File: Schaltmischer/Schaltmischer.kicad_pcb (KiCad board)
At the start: 2 copper layers, 13 parts, among them P1 Power, P2 IN, P3 Takt, P4 OUT, T1 Übertrager, T2 Übertrager, U1 FST3125

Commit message: Schaltplan Rev D, Layout Rev A
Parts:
- C1: footprint Capacitors_THT:C_Radial_D6.3_L11.2_P2.5 -> Discret:C1V7H_2
- C2, C3, C4, R1, R2: moved to B.Cu
- moved P1 30.6 mm to (116.8, 96.5)
- moved C4 29.6 mm to (117.4, 92.7)
- moved R1 23.7 mm to (125.1, 94.5), turned to 270 degrees
- moved R2 23.4 mm to (112.4, 94.5), turned to 90 degrees
- moved C3 22.1 mm to (130.8, 88.9)
- moved C1 19.1 mm to (120.7, 90.2), turned to 180 degrees
- moved C2 18.2 mm to (108.0, 88.9), turned to 180 degrees
- moved P3 15.2 mm to (116.8, 73.7)
- moved P4 5.08 mm to (137.2, 81.3)
- moved P2 5.08 mm to (104.1, 81.3)
- moved T1 4.02 mm to (111.8, 82.5), turned to 0 degrees
- moved T2 4.02 mm to (129.5, 82.5), turned to 180 degrees
- moved U1 1.80 mm to (120.7, 82.5)
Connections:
- T1 pad 2: GND -> Net-(C1-Pad1)
- T1 pad 5: Net-(C1-Pad1) -> Net-(T1-Pad5)
- T1 pad 6: Net-(T1-Pad6) -> GND
- T2 pad 1: OUT -> GND
- T2 pad 2: GND -> Net-(C1-Pad1)
- T2 pad 5: Net-(C1-Pad1) -> Net-(T2-Pad5)
- T2 pad 6: Net-(T2-Pad6) -> OUT
- U1 pad 1: SW1 -> SW2
- U1 pad 11: Net-(T2-Pad6) -> Net-(T2-Pad3)
- U1 pad 12: Net-(T1-Pad6) -> Net-(T1-Pad5)
- U1 pad 13: IN1 -> SW1
- U1 pad 2: Net-(T1-Pad3) -> Net-(T1-Pad5)
- U1 pad 3: Net-(T2-Pad3) -> Net-(T2-Pad5)
- U1 pad 4: SW2 -> SW1
- U1 pad 6: Net-(T2-Pad6) -> Net-(T2-Pad5)
- U1 pad 9: Net-(T1-Pad6) -> Net-(T1-Pad3)
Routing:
- net GND: track 0.00 -> 118.9 mm, vias 0 -> 1
- net Net-(C1-Pad1): track 0.00 -> 52.4 mm
- net SW1: track 0.00 -> 20.9 mm, vias 0 -> 1
- net Net-(T1-Pad3): track 0.00 -> 18.5 mm, vias 0 -> 1
- net SW2: track 0.00 -> 17.9 mm, vias 0 -> 2
- net Net-(T1-Pad5): track 0.00 -> 17.7 mm
- net Net-(T2-Pad5): track 0.00 -> 17.1 mm
- net Net-(T2-Pad3): track 0.00 -> 13.5 mm
- net +5V: track 0.00 -> 8.86 mm
- net IN: track 0.00 -> 6.13 mm
- net OUT: track 0.00 -> 6.13 mm
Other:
- net class Default: clearance 0.2 -> 0.2032; trace_width 0.25 -> 0.2032; via_dia 0.6 -> 0.8128; via_drill 0.4 -> 0.4064
- rule trace_clearance: 0.2 -> 0.2032
- rule trace_min: 0.2 -> 0.2032
- rule via_min_drill: 0.3 -> 0.381
- rule via_min_size: 0.4 -> 0.762

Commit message: save before gnd floating
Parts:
- added P5: GND, Mounting_Holes:MountingHole_3.2mm_M3_Pad_Via, F.Cu at (104.6, 74.3)
- added P6: GND, Mounting_Holes:MountingHole_3.2mm_M3_Pad_Via, F.Cu at (136.6, 74.3)
- added P7: GND, Mounting_Holes:MountingHole_3.2mm_M3_Pad_Via, F.Cu at (136.6, 96.3)
- added P8: GND, Mounting_Holes:MountingHole_3.2mm_M3_Pad_Via, F.Cu at (104.6, 96.3)
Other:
- board outline added: 40 x 30 mm

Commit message: save after gnd floating
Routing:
- net GND: track 118.9 -> 2.07 mm
- net +5V: track 8.86 -> 10.6 mm
- added copper zone on B.Cu, net GND
- added copper zone on F.Cu, net GND
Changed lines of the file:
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@@
   (general
     (links 40)
-    (no_connects 4)
-    (area 100.064999 70.204999 141.215001 100.355001)
+    (no_connects 6)
+    (area 100.564999 70.204999 140.715001 100.355001)
     (thickness 1.6)
-    (drawings 15)
-    (tracks 105)
+    (drawings 16)
+    (tracks 84)
     (zones 0)
     (modules 17)
@@
   )
   (setup
-    (last_trace_width 0.2032)
+    (last_trace_width 1.016)
     (user_trace_width 0.254)
     (user_trace_width 0.4064)
@@
     (user_trace_width 1.016)
     (trace_clearance 0.2032)
-    (zone_clearance 0.508)
-    (zone_45_only no)
+    (zone_clearance 0.4)
+    (zone_45_only yes)
     (trace_min 0.2032)
     (segment_width 0.2)
@@
     (pad "" thru_hole circle (at 1.697056 -1.697056) (size 0.6 0.6) (drill 0.5) (layers *.Cu *.Mask))
   )
+  (gr_line (start 116.84 85.09) (end 116.84 86.995) (layer B.Mask) (width 1.016))
   (dimension 7 (width 0.3) (layer Eco1.User)
     (gr_text "7,0 mm" (at 144.99 77.78 90) (layer Eco1.User)
@@
   (gr_line (start 100.64 70.28) (end 140.64 70.28) (layer Edge.Cuts) (width 0.15))
   (gr_line (start 116.84 85.09) (end 115.57 92.71) (layer B.SilkS) (width 1.016))
-  (segment (start 137.16 83.82) (end 134.62 83.82) (width 1.016) (layer B.Cu) (net 1))
-  (segment (start 134.62 83.82) (end 132.08 86.36) (width 1.016) (layer B.Cu) (net 1))
-  (segment (start 132.81 88.9) (end 132.81 87.09) (width 1.016) (layer B.Cu) (net 1))
-  (segment (start 132.81 87.09) (end 132.08 86.36) (width 1.016) (layer B.Cu) (net 1))
-  (segment (start 124.46 87.63) (end 128.905 92.075) (width 0.2032) (layer F.Cu) (net 1))
-  (segment (start 124.46 81.915) (end 124.46 87.63) (width 0.2032) (layer F.Cu) (net 1))
+  (via (at 124.46 81.915) (size 1.2) (drill 0.6) (layers F.Cu B.Cu) (net 1))
   (segment (start 124.46 79.85) (end 124.46 81.915) (width 1.016) (layer B.Cu) (net 1))
-  (via (at 124.46 81.915) (size 1.2) (drill 0.6) (layers F.Cu B.Cu) (net 1))
-  (segment (start 104.14 83.82) (end 106.68 83.82) (width 0.2032) (layer F.Cu) (net 1))
-  (segment (start 106.68 83.82) (end 119.38 96.52) (width 0.2032) (layer F.Cu) (net 1))
-  (segment (start 127.635 71.12) (end 134.62 78.105) (width 0.2032) (layer F.Cu) (net 1))
-  (segment (start 119.38 73.66) (end 121.92 71.12) (width 0.2032) (layer F.Cu) (net 1))
-  (segment (start 121.92 71.12) (end 127.635 71.12) (width 0.2032) (layer F.Cu) (net 1))
-  (segment (start 124.46 96.52) (end 134.62 86.36) (width 0.2032) (layer F.Cu) (net 1))
-  (segment (start 134.62 86.36) (end 137.16 83.82) (width 0.2032) (layer F.Cu) (net 1))
-  (segment (start 134.62 78.105) (end 134.62 86.36) (width 0.2032) (layer F.Cu) (net 1))
-  (segment (start 119.38 96.52) (end 124.46 96.52) (width 0.2032) (layer F.Cu) (net 1))
-  (segment (start 121.92 92.71) (end 121.92 93.98) (width 1.016) (layer B.Cu) (net 1))
-  (segment (start 121.92 93.98) (end 119.38 96.52) (width 1.016) (layer B.Cu) (net 1))
-  (segment (start 119.38 96.52) (end 125.095 96.52) (width 1.016) (layer B.Cu) (net 1))
-  (segment (start 119.38 96.52) (end 119.38 92.71) (width 1.016) (layer B.Cu) (net 1))
-  (segment (start 105.95 88.9) (end 106.68 88.9) (width 1.016) (layer B.Cu) (net 1))
-  (segment (start 106.68 88.9) (end 109.22 86.36) (width 1.016) (layer B.Cu) (net 1))
-  (segment (start 104.14 83.82) (end 106.68 83.82) (width 1.016) (layer B.Cu) (net 1))
-  (segment (start 106.68 83.82) (end 109.22 86.36) (width 1.016) (layer B.Cu) (net 1))
+  (segment (start 119.38 90.17) (end 113.03 90.17) (width 1.016) (layer B.Cu) (net 2))
+  (segment (start 124.46 90.17) (end 119.38 90.17) (width 1.016) (layer B.Cu) (net 2))
   (segment (start 127.54 90.17) (end 125.095 90.17) (width 1.016) (layer B.Cu) (net 2))
   (segment (start 125.095 90.17) (end 124.46 90.17) (width 1.016) (layer B.Cu) (net 2))
@@
   (segment (start 112.395 92.52) (end 112.395 90.17) (width 1.016) (layer B.Cu) (net 2))
   (segment (start 112.395 90.17) (end 111.22 90.17) (width 1.016) (layer B.Cu) (net 2))
-  (segment (start 124.46 90.17) (end 113.03 90.17) (width 1.016) (layer B.Cu) (net 2))
   (segment (start 128.81 88.9) (end 127.54 90.17) (width 1.016) (layer B.Cu) (net 2))
   (segment (start 111.22 90.17) (end 109.95 88.9) (width 1.016) (layer B.Cu) (net 2))
@@
   (segment (start 127 78.74) (end 127 81.28) (width 1.016) (layer B.Cu) (net 2))
   (segment (start 127 81.28) (end 129.54 83.82) (width 1.016) (layer B.Cu) (net 2))
+  (segment (start 116.84 85.25) (end 116.84 86.995) (width 1.016) (layer B.Cu) (net 3))
   (segment (start 112.395 96.52) (end 116.84 96.52) (width 1.016) (layer B.Cu) (net 3))
   (segment (start 116.84 96.52) (end 116.84 94.17) (width 1.016) (layer B.Cu) (net 3))
@@
   (segment (start 129.54 78.74) (end 129.54 77.67934) (width 1.016) (layer B.Cu) (net 11))
   (segment (start 129.54 77.67934) (end 128.69566 76.835) (width 1.016) (layer B.Cu) (net 11))
+  (zone (net 1) (net_name GND) (layer F.Cu) (hatch edge 0.508)
+    (connect_pads yes (clearance 0.4))
+    (min_thickness 1.5)
+    (fill yes (arc_segments 16) (thermal_gap 0.508) (thermal_bridge_width 0.508) (smoothing fillet))
+    (polygon
+      (pts
+        (xy 100.64 70.28) (xy 140.64 70.28) (xy 140.64 100.28) (xy 100.64 100.28)
+      )
+    )
+  )
+  (zone (net 1) (net_name GND) (layer B.Cu) (hatch edge 0.508)
+    (connect_pads yes (clearance 0.4))
+    (min_thickness 1.5)
+    (fill yes (arc_segments 16) (thermal_gap 0.508) (thermal_bridge_width 0.508) (smoothing fillet))
+    (polygon
+      (pts
+        (xy 100.64 70.28) (xy 140.64 70.28) (xy 140.64 100.28) (xy 100.64 100.28)
+      )
+    )
+  )
+  (zone (net 0) (net_name "") (layer B.Cu) (hatch edge 0.508)
+    (connect_pads yes (clearance 0.4))
+    (min_thickness 1.5)
+    (keepout (tracks allowed) (vias allowed) (copperpour not_allowed))
+    (fill yes (arc_segments 16) (thermal_gap 0.508) (thermal_bridge_width 0.508) (smoothing fillet))
+    (polygon
+      (pts
+        (xy 110.49 86.36) (xy 130.81 86.36) (xy 130.81 83.82) (xy 133.35 83.82) (xy 133.35 77.47)
+        (xy 107.95 77.47) (xy 107.95 83.82) (xy 110.49 83.82)
+      )
+    )
+  )
 )

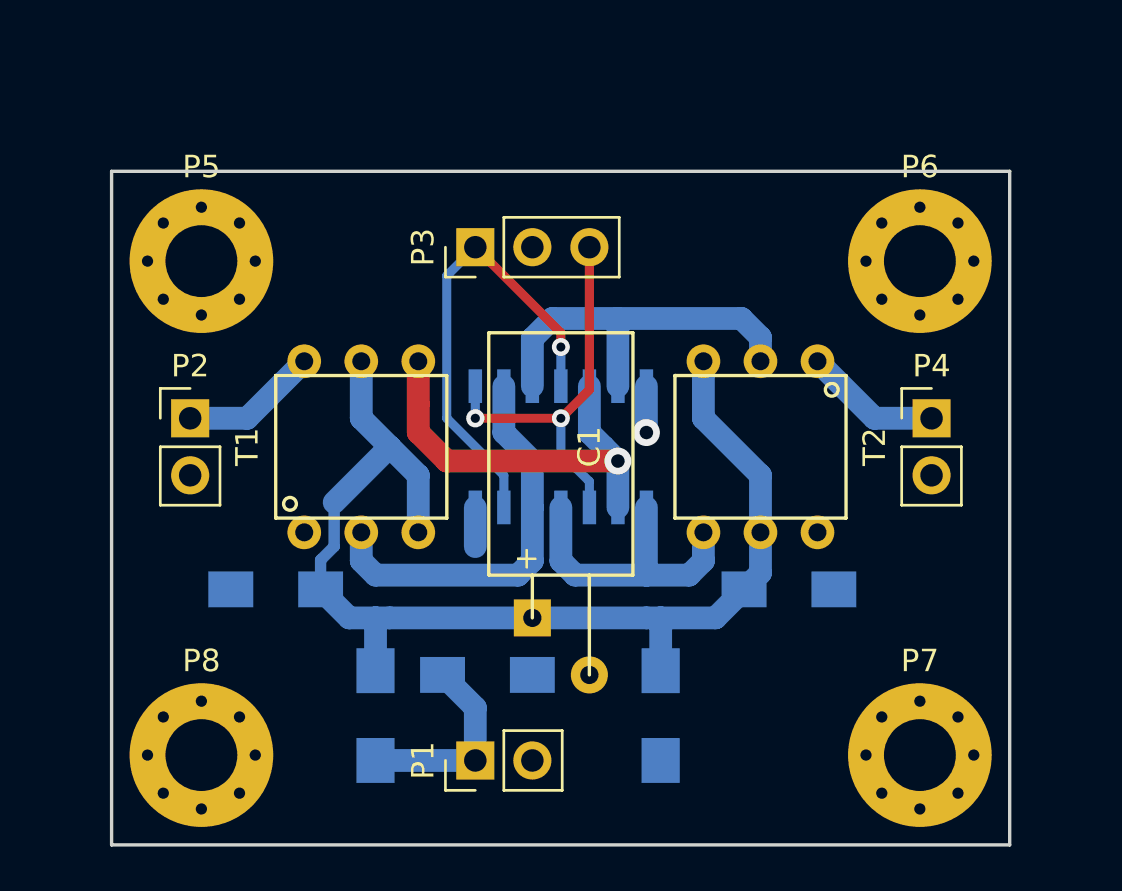
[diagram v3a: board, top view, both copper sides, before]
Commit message: Sicherung vor Trafo wechsel im layout
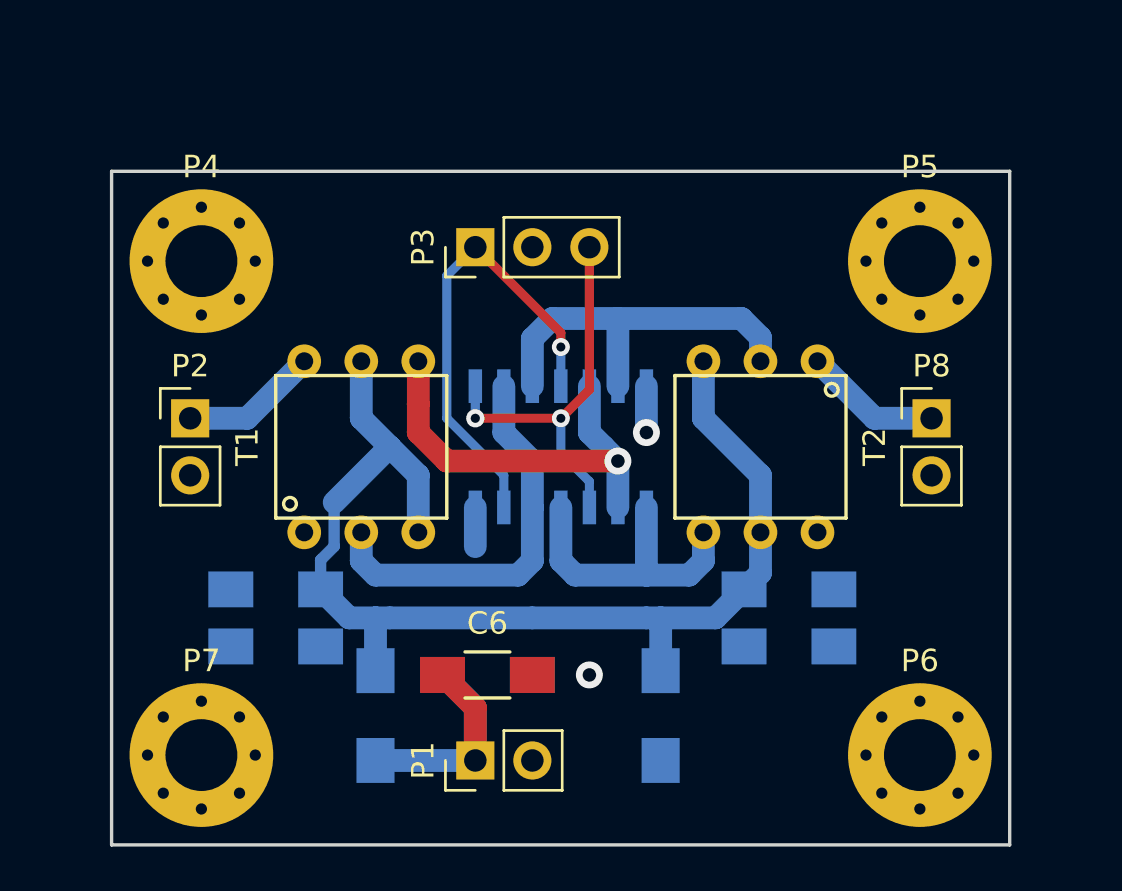
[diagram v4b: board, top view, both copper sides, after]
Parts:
- added C3: 1µ, Capacitors_SMD:C_1206_HandSoldering, B.Cu at (130.8, 91.4)
- added C6: 10µ, Capacitors_SMD:C_1206_HandSoldering, F.Cu at (117.4, 92.7)
- C1: value 10µ -> 10n; footprint Discret:C1V7H_2 -> Capacitors_SMD:C_1206_HandSoldering; moved to B.Cu
- C2: value 10n -> 1µ
- C5: renamed from C4; value 100n -> 10n
- moved C1 12.8 mm to (108.0, 88.9)
- moved C2 2.54 mm to (108.0, 91.4)
- renumbered C3 to C4, P5 to P4, P6 to P5, P7 to P6, P8 to P7, P4 to P8, R2 to R1, R1 to R2
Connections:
- T2 pad 1: GND -> OUT
- T2 pad 6: OUT -> GND
- U1 pad 11: Net-(T2-Pad3) -> Net-(T2-Pad5)
- U1 pad 3: Net-(T2-Pad5) -> Net-(T2-Pad3)
- U1 pad 6: Net-(T2-Pad5) -> Net-(T2-Pad3)
- U1 pad 8: Net-(T2-Pad3) -> Net-(T2-Pad5)
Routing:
- net Net-(T2-Pad3): track 13.5 -> 24.2 mm
- net Net-(T2-Pad5): track 17.1 -> 6.46 mm
- net +5V: track 10.6 -> 15.0 mm
- net OUT: track 6.13 -> 2.54 mm
- net GND: track 2.07 -> 5.66 mm
- net (no net): vias 0 -> 1

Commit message: Schaltplan Rev E; Layout Rev B
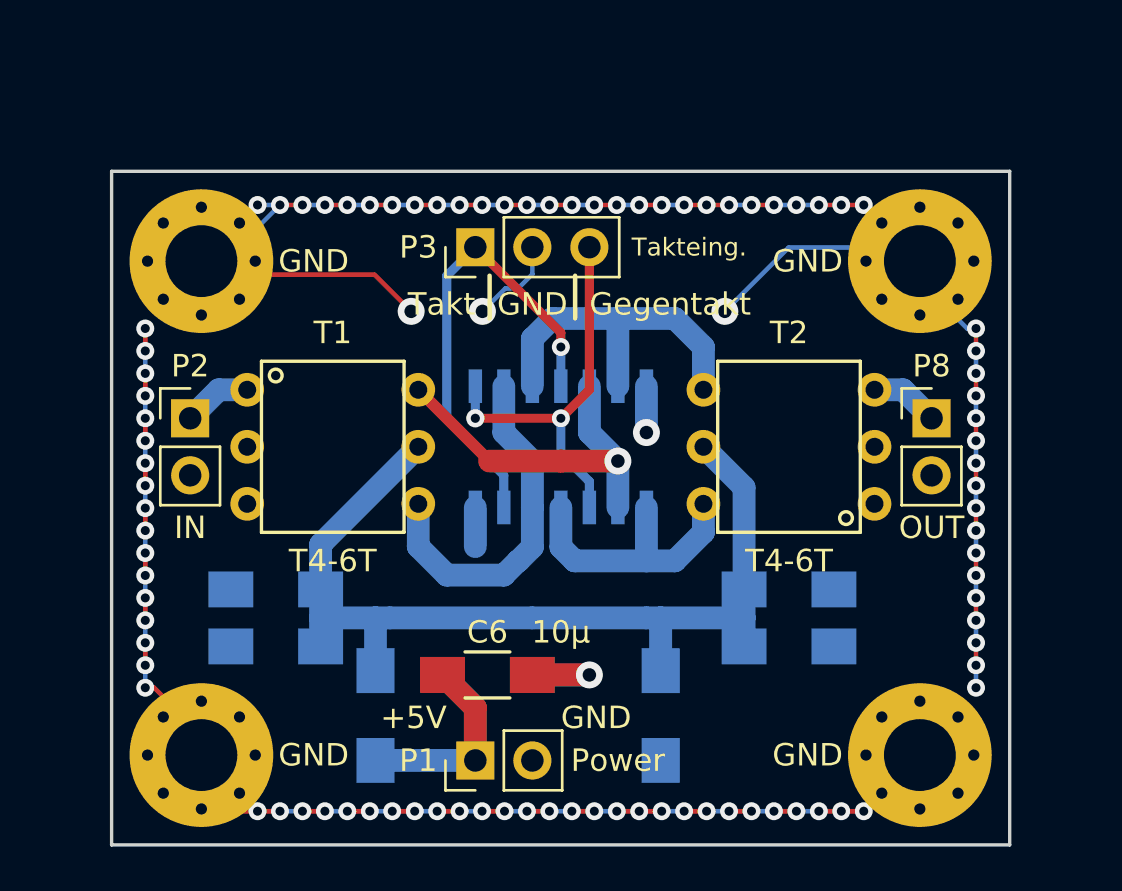
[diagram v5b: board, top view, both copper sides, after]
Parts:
- P3: value Takt -> Takteing.
- T1, T2: value Übertrager -> T4-6T
- moved T1 1.27 mm to (110.5, 82.5), turned to 270 degrees
- moved T2 1.27 mm to (130.8, 82.5), turned to 90 degrees
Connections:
- T1 pad 1: IN -> Net-(T1-Pad1)
- T1 pad 4: Net-(C1-Pad1) -> GND
- T1 pad 5: Net-(T1-Pad5) -> (no net)
- T1 pad 6: GND -> IN
- T2 pad 1: OUT -> Net-(T2-Pad1)
- T2 pad 4: Net-(C1-Pad1) -> OUT
- T2 pad 5: Net-(T2-Pad5) -> (no net)
- U1 pad 11: Net-(T2-Pad5) -> Net-(T2-Pad1)
- U1 pad 12: Net-(T1-Pad5) -> Net-(T1-Pad3)
- U1 pad 2: Net-(T1-Pad5) -> Net-(T1-Pad3)
- U1 pad 5: Net-(T1-Pad3) -> Net-(T1-Pad1)
- U1 pad 8: Net-(T2-Pad5) -> Net-(T2-Pad1)
- U1 pad 9: Net-(T1-Pad3) -> Net-(T1-Pad1)
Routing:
- net GND: track 5.66 -> 134.8 mm, vias 1 -> 95
- net Net-(T1-Pad5): track 17.7 -> 0.00 mm
- net Net-(T1-Pad1): track 0.00 -> 16.1 mm, vias 0 -> 1
- net Net-(T2-Pad1): track 0.00 -> 12.5 mm
- net Net-(T2-Pad3): track 24.2 -> 15.6 mm
- net Net-(C1-Pad1): track 52.4 -> 43.9 mm
- net Net-(T2-Pad5): track 6.46 -> 0.00 mm
- net IN: track 6.13 -> 3.07 mm
- net Net-(T1-Pad3): track 18.5 -> 15.7 mm, vias 1 -> 0
- net OUT: track 2.54 -> 3.07 mm
- net (no net): vias 1 -> 0
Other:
- board text added: "+5V"
- board text added: "GND"
- board text added: "Gegentakt"
- board text added: "Takt"
